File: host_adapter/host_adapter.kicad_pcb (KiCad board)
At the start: 2 copper layers, 208.2 x 40.9 mm, 7 parts, among them J1 Conn_01x40_Male, J2 Conn_01x40_Male, J3 Conn_01x02_Male, J4 Connector_PCIe_x16, J5 Conn_01x40_Male, J6 Conn_01x40_Male, J7 Conn_01x02_Male

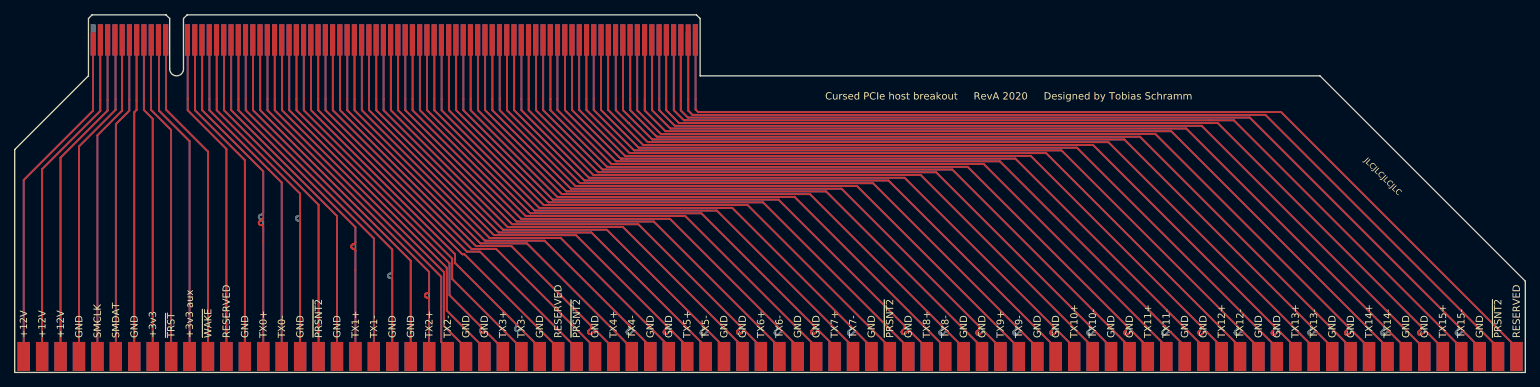
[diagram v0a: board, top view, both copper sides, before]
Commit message: Deepen PCIe x16 slot cutout
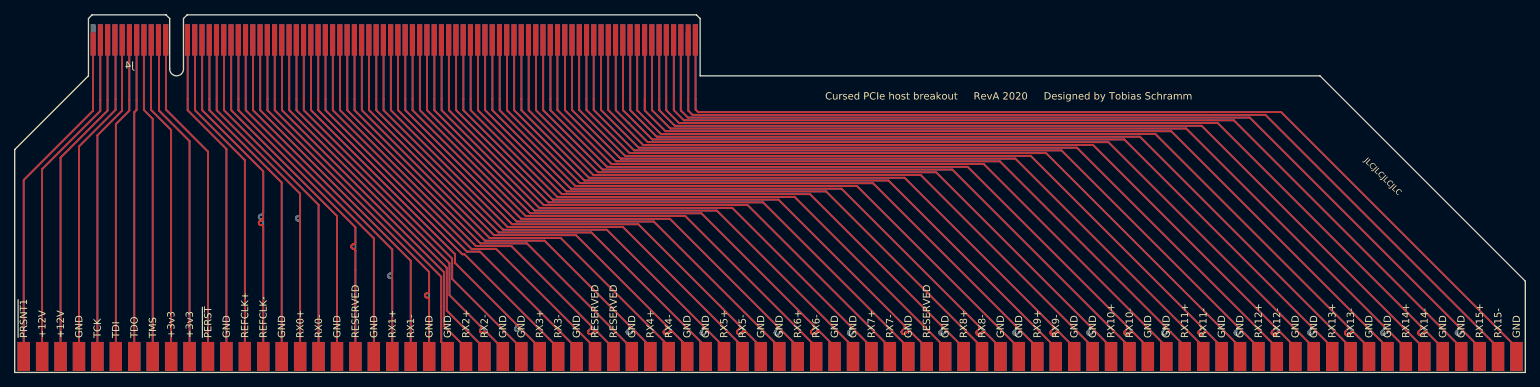
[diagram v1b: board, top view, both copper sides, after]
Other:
- net class Default: clearance 0.2 -> 0.127
- rule trace_clearance: 0.2 -> 0.127
- rule trace_min: 0.2 -> 0.127
